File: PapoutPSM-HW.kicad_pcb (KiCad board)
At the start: 4 copper layers, 100 x 45 mm, 104 parts, among them J1 53015-0510, J2 53015-0510, U1 STM32G031F8P6, U10 RT8259GJ6, U2 SP3232EEY-L, U3 LTV-817S, U4 LTV-817S, U5 LTV-817S, U6 LTV-817S, U7 LTV-817S, U8 LTV-817S, U9 LMR14050SDDA

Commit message: clean up some
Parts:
- moved U10 71.2 mm to (146.3, 60.5)
- moved C34 71.2 mm to (148.6, 60.0)
- moved D12 71.2 mm to (157.9, 59.2)
- moved L3 71.2 mm to (152.5, 59.0)
- moved R27 71.2 mm to (147.0, 56.0)
- moved R28 71.2 mm to (145.3, 56.0)
- moved C31 71.2 mm to (148.2, 64.0)
- moved C32 71.2 mm to (143.7, 63.3)
- moved C33 71.2 mm to (143.7, 60.2)
- moved R29 71.2 mm to (143.7, 56.0)
- moved C17 5.72 mm to (69.1, 61.4)
- moved R23 5.72 mm to (71.3, 61.4)
- moved C9 4.38 mm to (69.1, 66.4)
- moved R3 4.38 mm to (71.3, 66.4)
- moved C16 3.74 mm to (69.1, 62.4)
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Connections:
- U1 pad 11: /P_INHIBIT -> /P_ERROR
- U1 pad 12: /P_RESET -> /P_EMPTY
- U1 pad 13: /P_PULSE -> /P_OUT_PULSE
- U1 pad 14: /P_OUT_PULSE -> /P_PULSE
- U1 pad 15: /P_EMPTY -> /P_RESET
- U1 pad 16: /P_ERROR -> /P_INHIBIT
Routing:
- net /P_OUT_PULSE: track 13.2 -> 3.35 mm
- net /P_RESET: track 1.34 -> 2.14 mm
- net /P_PULSE: track 2.14 -> 1.34 mm
- net /P_INHIBIT: track 2.14 -> 1.34 mm
- net +3V3: vias 10 -> 9
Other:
- board text added: "2021.10.xx"
- board text added: "Paper Dispenser Serialize Adapter v0.4"
- board text removed: "2021.09.01"
- board text removed: "Paper Dispenser Serialize Adapter v0.3"

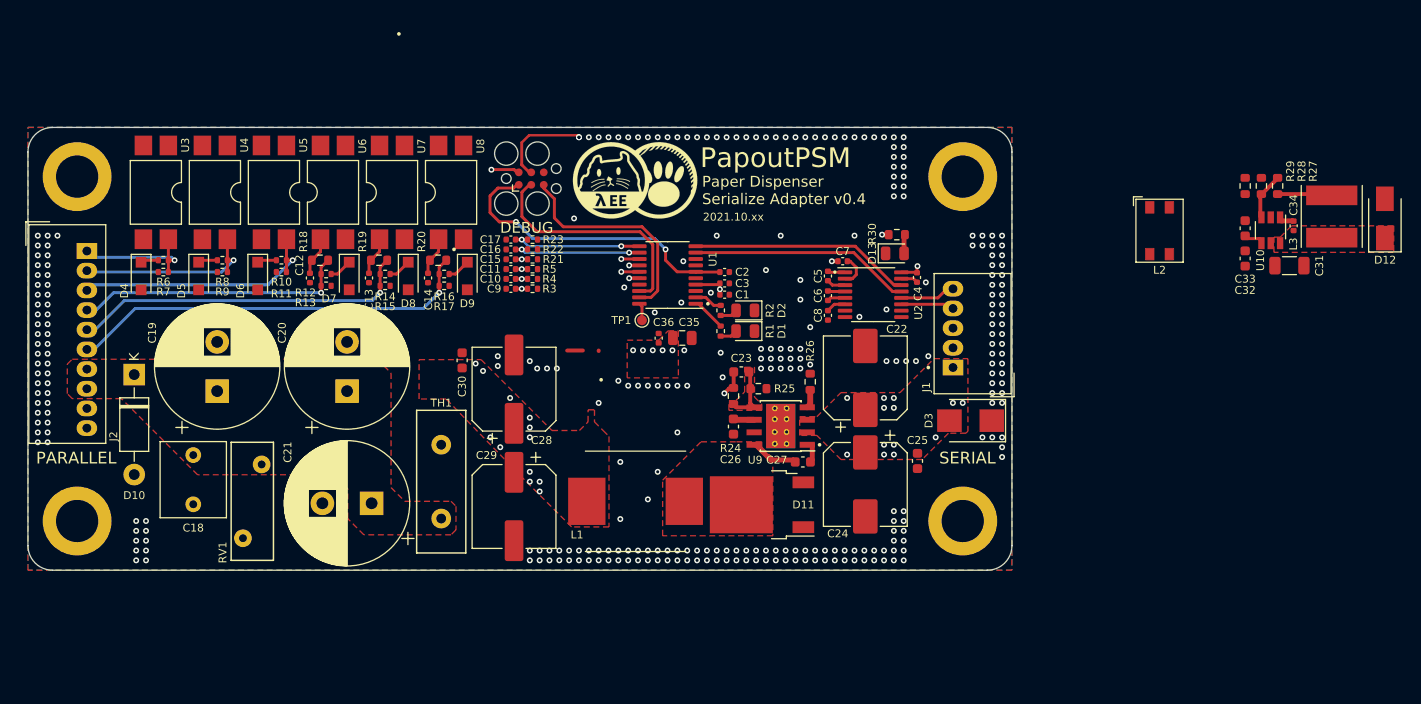
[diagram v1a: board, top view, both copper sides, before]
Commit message: some layout changed (sizeup for later 2layer conversion)
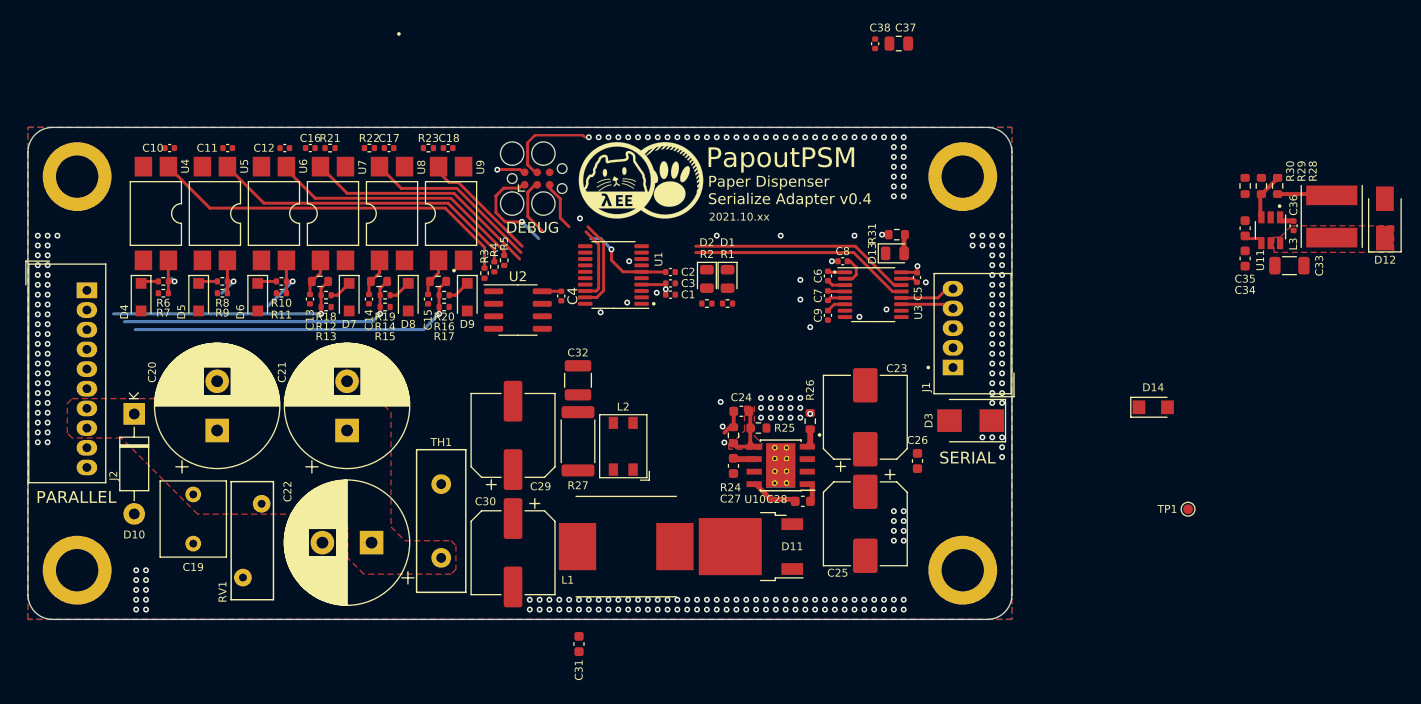
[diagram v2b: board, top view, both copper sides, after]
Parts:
- added C32: 33nF Film, Capacitor_SMD:C_1210_3225Metric, F.Cu at (75.9, 75.7)
- added C4: 100nF, Capacitor_SMD:C_0402_1005Metric, F.Cu at (74.2, 67.1)
- added D14: MSP3V3-M3/89A, Diode_SMD:D_SMF, F.Cu at (134.4, 78.4)
- added R27: 33 2W, Resistor_SMD:R_2512_6332Metric, F.Cu at (75.9, 81.9)
- added U2: MB85RS64, Package_SO:SOIC-8_3.9x4.9mm_P1.27mm, F.Cu at (69.8, 68.6)
- D11: value MBRD20150CT-13 -> MBRD20150CT
- L2: value L_Coupled_1243 -> ACM4520-142-2P-T000
- moved L2 58.7 mm to (80.5, 82.4), turned to 180 degrees
- moved TP1 58.7 mm to (137.9, 88.8)
- moved C10 37.5 mm to (34.4, 52.1)
- moved C37 37.1 mm to (108.5, 41.5)
- moved C38 37.1 mm to (106.1, 41.5)
- moved C11 31.7 mm to (40.3, 52.1)
- moved C31 31.2 mm to (76.0, 102.5)
- moved C12 26.1 mm to (46.1, 52.1)
- moved R21 23.5 mm to (50.7, 52.1)
- moved C16 23.3 mm to (48.7, 52.1)
- moved R22 19.5 mm to (54.7, 52.1), turned to 180 degrees
- moved C17 16.1 mm to (56.7, 52.1), turned to 0 degrees
- moved R23 14.1 mm to (60.7, 52.1), turned to 180 degrees
- moved C18 11.3 mm to (62.7, 52.1), turned to 0 degrees
- moved D1 5.60 mm to (91.1, 65.4), turned to -90 degrees
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- renumbered C9 to C10, C10 to C11, C11 to C12, C12 to C13, C13 to C14, C14 to C15, C15 to C16, C16 to C17, C17 to C18, C18 to C19, C19 to C20, C20 to C21, C21 to C22, C22 to C23, C23 to C24, C24 to C25, C25 to C26, C26 to C27, C27 to C28, C28 to C29, C29 to C30, C30 to C31, C31 to C33, C32 to C34, C33 to C35, C34 to C36, C35 to C37, C36 to C38, C4 to C5, C5 to C6, C6 to C7, C7 to C8, C8 to C9, R27 to R28, R28 to R29, R29 to R30, R30 to R31, U9 to U10, U10 to U11, U2 to U3, U3 to U4, U4 to U5, U5 to U6, U6 to U7, U7 to U8, U8 to U9
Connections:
- L2 pad 1: +12V -> GNDPWR
- L2 pad 2: +12VA -> +12V
- L2 pad 3: GND -> +12VA
- L2 pad 4: GNDPWR -> GND
- TP1 pad 1: /TEST_POINT -> (no net)
- U1 pad 17: GND -> /FRAM_MOSI
- U1 pad 20: /TEST_POINT -> /FRAM_MISO
- U1 pad 7: GND -> (no net)
- U1 pad 8: GND -> /FRAM_SCK
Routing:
- net Net-(C10-Pad1): track 1.21 -> 37.6 mm, vias 1 -> 0
- net Net-(C11-Pad1): track 1.21 -> 31.9 mm, vias 1 -> 0
- net Net-(C12-Pad1): track 1.19 -> 26.3 mm, vias 1 -> 0
- net /P_OUT_PULSE: track 3.35 -> 24.1 mm, vias 2 -> 0
- net /Parallel_IO/J_PULSE: track 26.1 -> 7.50 mm
- net /Parallel_IO/J_RESET: track 19.4 -> 5.66 mm
- net /NRST: track 31.4 -> 20.0 mm
- net /SWDIO: track 24.0 -> 13.5 mm
- net /Parallel_IO/J_INHIBIT: track 13.3 -> 4.39 mm
- net /SWCLK: track 22.5 -> 14.5 mm
- net /Parallel_IO/J_ERROR: track 41.8 -> 35.1 mm
- net /Parallel_IO/J_EMPTY: track 35.0 -> 29.9 mm
- net /P_EMPTY: track 13.6 -> 18.0 mm, vias 2 -> 0
- net /LED0: track 3.50 -> 0.00 mm
- net /Parallel_IO/J_OUT_PULSE: track 28.1 -> 24.7 mm
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- removed copper zone on F.Cu, net +12V
- removed copper zone on F.Cu, net +24V
- removed copper zone on In2.Cu, net +24V
- removed copper zone on F.Cu, net +3V3
- removed copper zone on F.Cu, net /Power/BIG_SW
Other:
- board size 100 x 45 mm -> 100 x 50 mm
